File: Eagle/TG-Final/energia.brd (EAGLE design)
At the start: 172.7 x 172.7 mm, 45 parts, among them IC1 7812T, IC2 7805, IC3 AZ1117, IC4 7806T, Q1 TIP2955

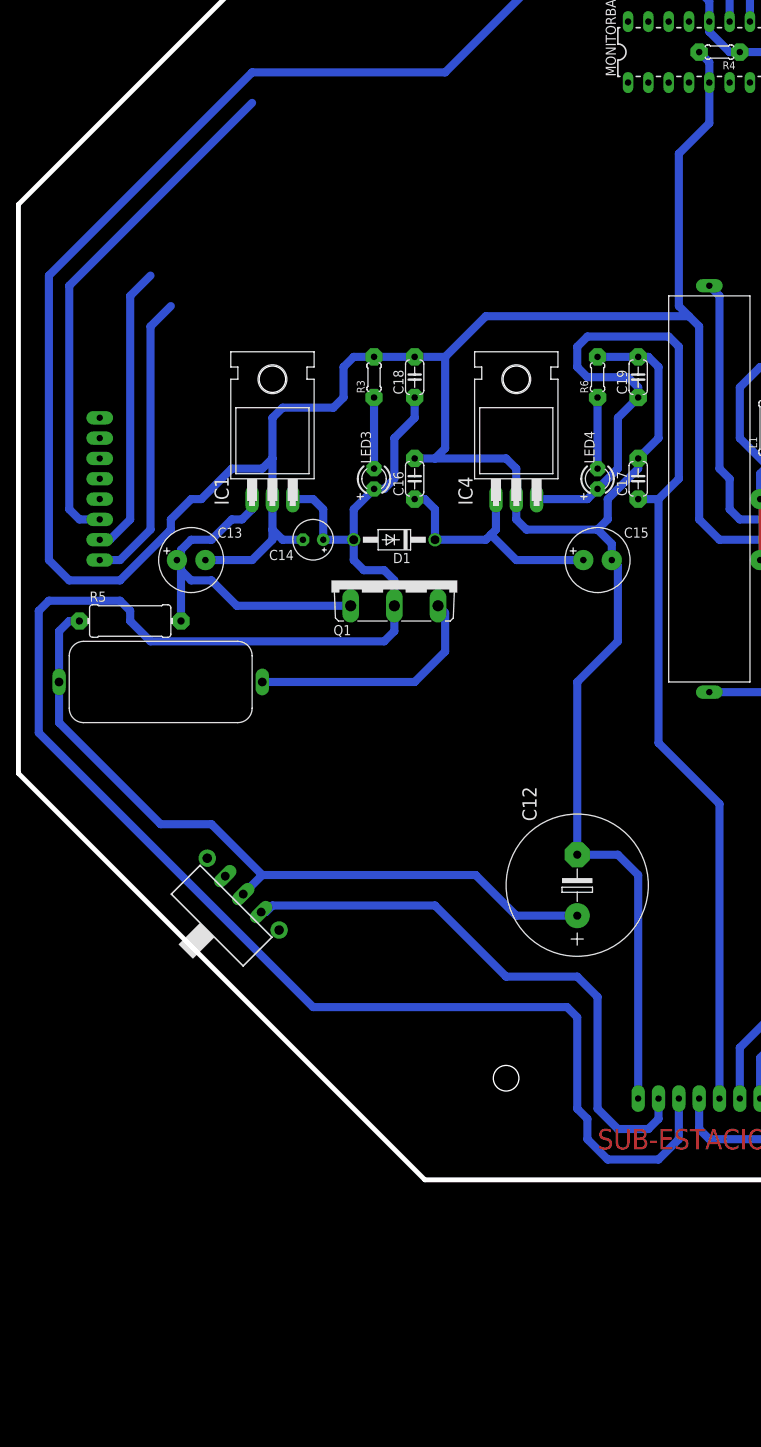
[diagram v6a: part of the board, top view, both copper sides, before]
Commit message: Pruebas del Monitor de Baterias Lipo
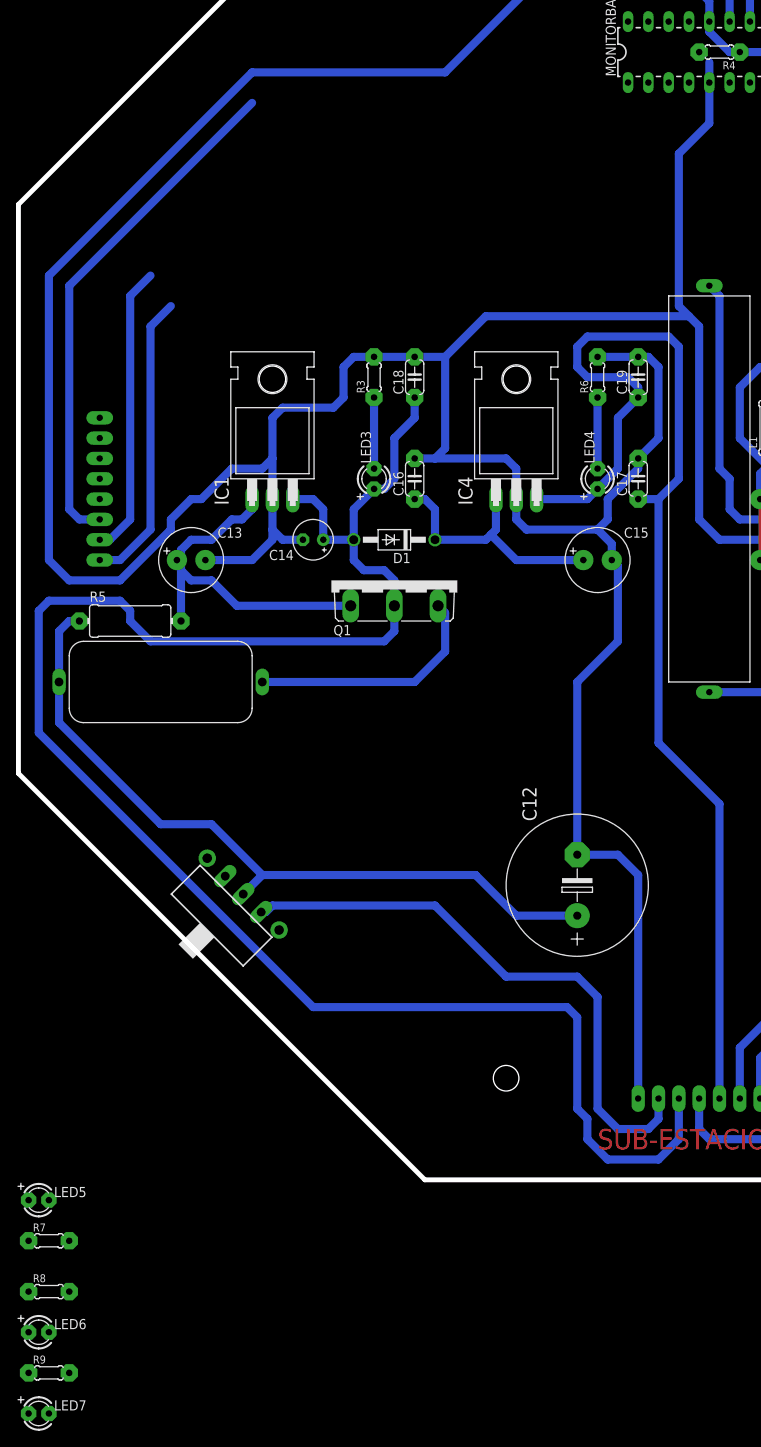
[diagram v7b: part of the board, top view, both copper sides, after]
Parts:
- added LED5, LED6, LED7: (no value), adafruit:LED3MM
- added R7, R8, R9: 470, rcl:0204/5
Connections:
- new net N$15: LED5.K, R7.2
- new net N$16: LED6.K, R8.2
- new net N$19: LED7.K, R9.2
- net N$2: now also R4.2
- net VSS: now also R7.1, R8.1, R9.1; no longer R4.2
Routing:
- net VSS: track 633.6 -> 631.8 mm
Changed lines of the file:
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@@
 <element name="LED4" library="adafruit" package="LED3MM" value="VERDE" x="21.59" y="87.63" rot="R90"/>
 <element name="R6" library="rcl" package="0204/5" value="680" x="21.59" y="100.33" rot="R90"/>
+<element name="LED5" library="adafruit" package="LED3MM" value="" x="-48.26" y="-2.54"/>
+<element name="R7" library="rcl" package="0204/5" value="470" x="-46.99" y="-7.62"/>
+<element name="LED6" library="adafruit" package="LED3MM" value="" x="-48.26" y="-19.05"/>
+<element name="R8" library="rcl" package="0204/5" value="470" x="-46.99" y="-13.97"/>
+<element name="LED7" library="adafruit" package="LED3MM" value="" x="-48.26" y="-29.21"/>
+<element name="R9" library="rcl" package="0204/5" value="470" x="-46.99" y="-24.13"/>
 </elements>
 <signals>
@@
 <contactref element="JP1" pad="4"/>
 <contactref element="MONITORBATERIA" pad="5"/>
-<contactref element="R4" pad="2"/>
 <contactref element="C18" pad="2"/>
 <contactref element="R3" pad="2"/>
@@
 <wire x1="57.15" y1="83.07605" x2="57.15" y2="85.09" width="1.016" layer="16"/>
 <wire x1="35.56" y1="137.16" x2="35.56" y2="139.7" width="1.016" layer="16"/>
-<wire x1="35.56" y1="139.7" x2="34.29" y2="140.97" width="1.016" layer="16"/>
 <wire x1="34.29" y1="152.4" x2="34.29" y2="154.94" width="1.016" layer="16"/>
 <wire x1="34.29" y1="154.94" x2="33.02" y2="156.21" width="1.016" layer="16"/>
@@
 <wire x1="33.02" y1="107.95" x2="31.75" y2="109.22" width="1.016" layer="16"/>
 <wire x1="31.75" y1="109.22" x2="31.75" y2="128.27" width="1.016" layer="16"/>
+<contactref element="R7" pad="1"/>
+<contactref element="R8" pad="1"/>
+<contactref element="R9" pad="1"/>
+<wire x1="-49.53" y1="-13.97" x2="-49.53" y2="-24.13" width="0" layer="19" extent="1-1"/>
+<wire x1="-49.53" y1="-7.62" x2="-49.53" y2="-13.97" width="0" layer="19" extent="1-1"/>
+<wire x1="26.67" y1="10.16" x2="-49.53" y2="-7.62" width="0" layer="19" extent="1-1"/>
 </signal>
 <signal name="+22V">
@@
 <contactref element="JP1" pad="6"/>
 <contactref element="MONITORBATERIA" pad="4"/>
-<wire x1="33.02" y1="137.16" x2="29.21" y2="152.4" width="0" layer="19" extent="1-1"/>
+<contactref element="R4" pad="2"/>
+<wire x1="34.29" y1="140.97" x2="29.21" y2="152.4" width="0" layer="19" extent="1-1"/>
+<wire x1="33.02" y1="137.16" x2="34.29" y2="140.97" width="0" layer="19" extent="1-1"/>
 </signal>
 <signal name="N$5">
@@
 <wire x1="21.59" y1="97.79" x2="21.59" y2="88.9" width="1.016" layer="16"/>
 </signal>
+<signal name="N$15">
+<contactref element="LED5" pad="K"/>
+<contactref element="R7" pad="2"/>
+<wire x1="-46.99" y1="-2.54" x2="-44.45" y2="-7.62" width="0" layer="19" extent="1-1"/>
+</signal>
+<signal name="N$16">
+<contactref element="LED6" pad="K"/>
+<contactref element="R8" pad="2"/>
+<wire x1="-44.45" y1="-13.97" x2="-46.99" y2="-19.05" width="0" layer="19" extent="1-1"/>
+</signal>
+<signal name="N$19">
+<contactref element="LED7" pad="K"/>
+<contactref element="R9" pad="2"/>
+<wire x1="-44.45" y1="-24.13" x2="-46.99" y2="-29.21" width="0" layer="19" extent="1-1"/>
+</signal>
 </signals>

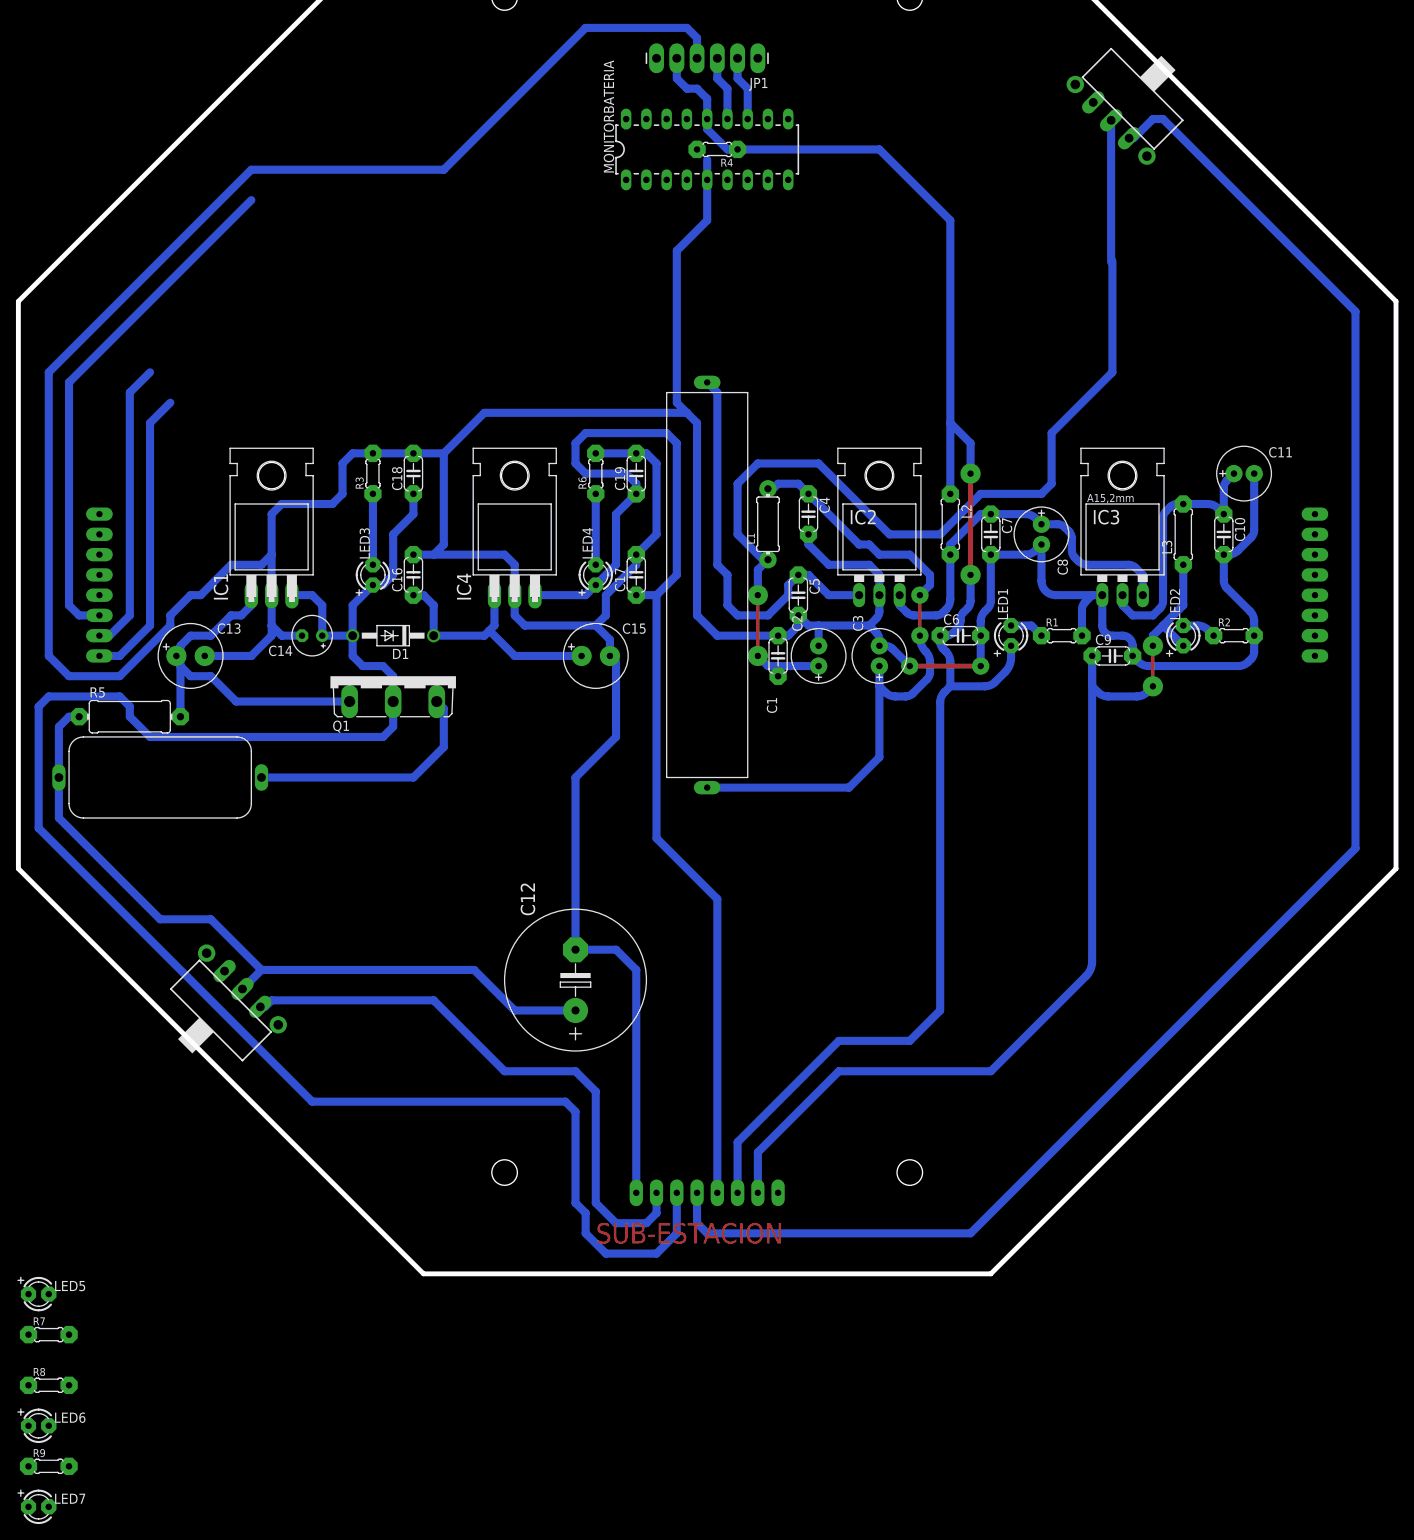
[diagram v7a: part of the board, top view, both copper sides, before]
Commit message: Peliando con un 16f88
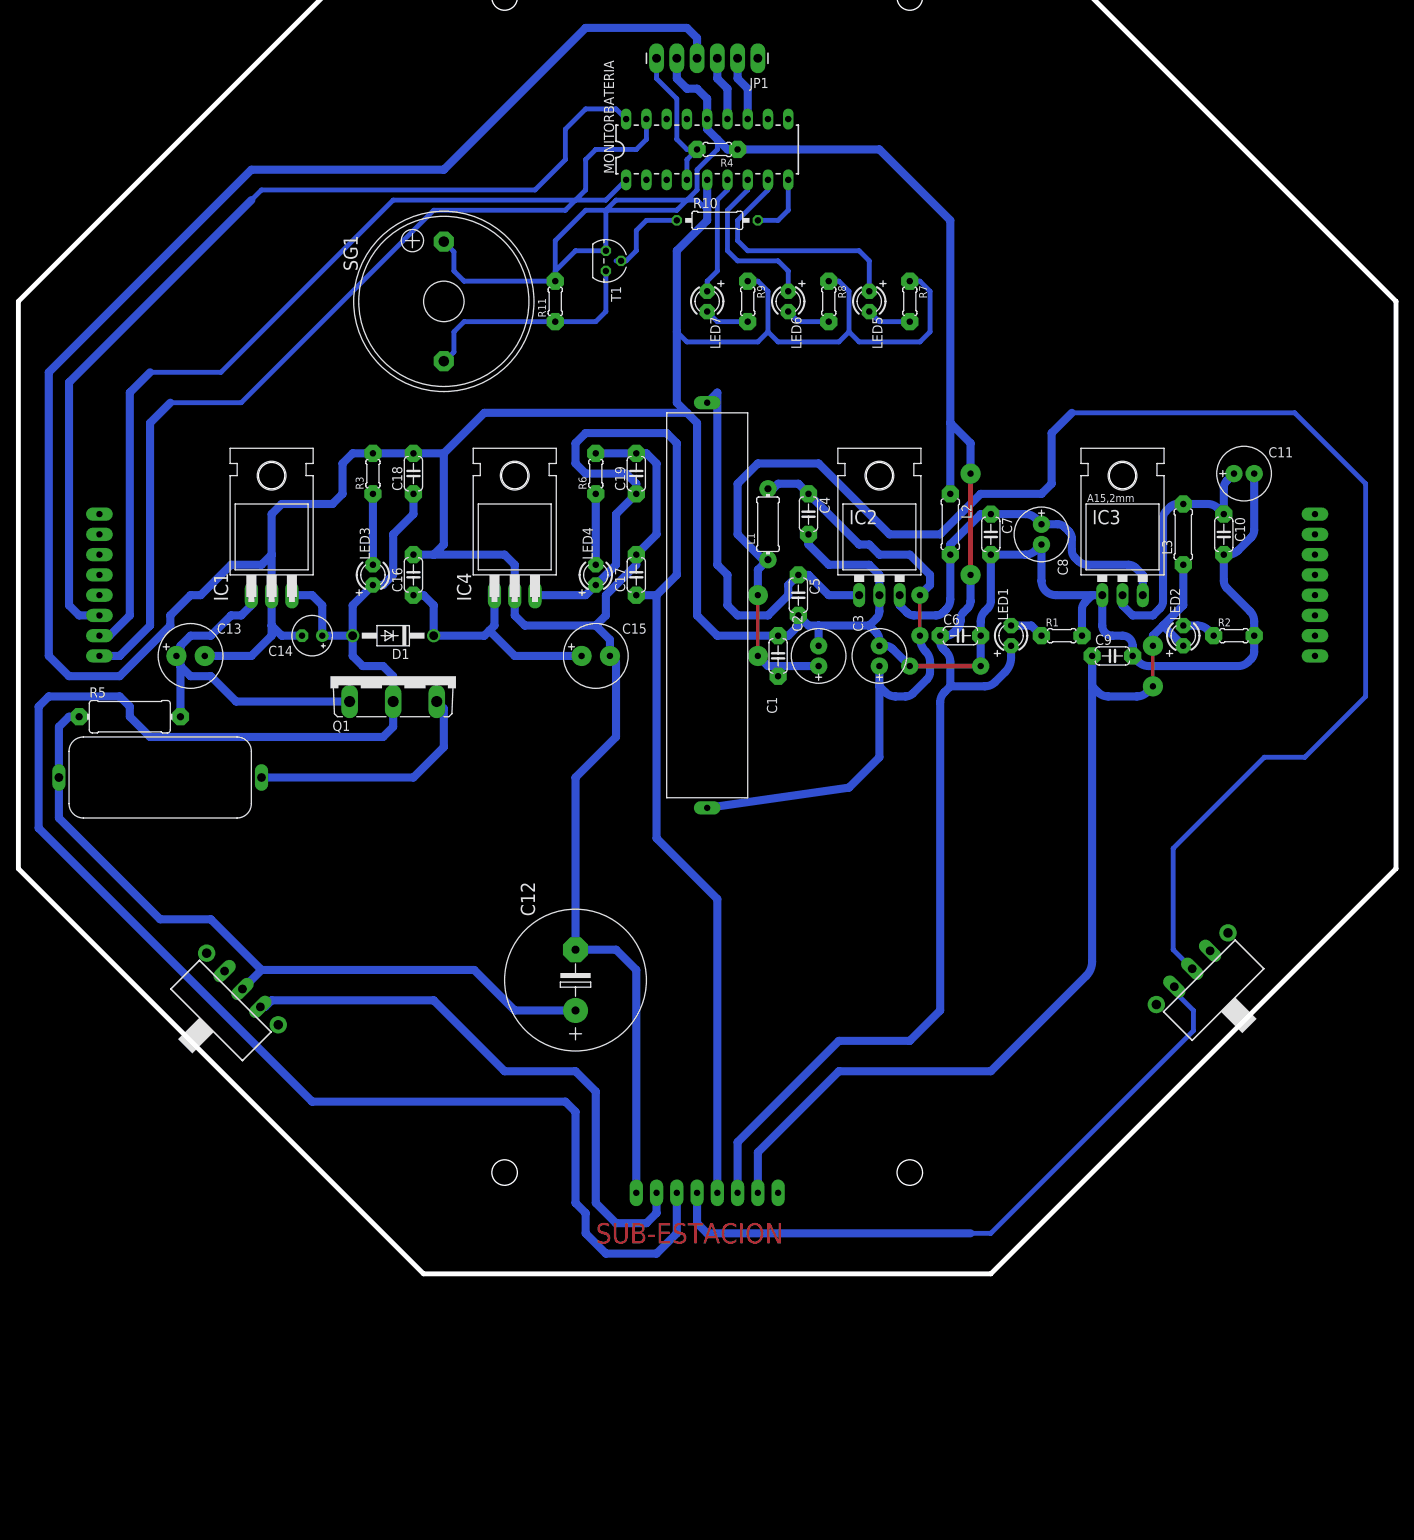
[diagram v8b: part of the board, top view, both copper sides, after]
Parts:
- added R10: 4K7, rcl:0207/10
- added R11: 4K7, rcl:0204/5
- added SG1: EB2209A, buzzer:EB2209A
- added T1: 2N3904, transistor:TO92
- moved LED7 172.8 mm to (35.6, 121.9), turned to 270 degrees
- moved R9 170.3 mm to (40.6, 121.9), turned to 270 degrees
- moved LED6 169.4 mm to (45.7, 121.9), turned to 270 degrees
- moved R7 168.6 mm to (61.0, 121.9), turned to 270 degrees
- moved R8 167.4 mm to (50.8, 121.9), turned to 270 degrees
- moved LED5 162.3 mm to (55.9, 121.9), turned to 270 degrees
- moved S1 112.2 mm to (99.1, 35.6), turned to 225 degrees
- moved U$9 2.54 mm to (35.6, 83.8)
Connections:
- new net N$20: LED7.A, MONITORBATERIA.6
- new net N$21: LED6.A, MONITORBATERIA.7
- new net N$22: LED5.A, MONITORBATERIA.8
- new net N$23: MONITORBATERIA.9, R10.2
- new net N$24: R10.1, T1.2
- new net N$25: R11.1, SG1.-, T1.1
- net VDD: now also R11.2, SG1.+
- net VSS: now also T1.3
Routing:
- net +11V1: track 213.6 -> 83.7 mm
- net SENSE1: track 36.9 -> 115.1 mm
- net N$1: track 129.1 -> 205.4 mm
- net VSS: track 631.8 -> 707.5 mm
- net SENSE3: track 36.4 -> 106.1 mm
- net VDD: track 207.7 -> 266.7 mm
- net SENSE2: track 64.6 -> 119.1 mm
- net N$22: track 0.00 -> 30.6 mm
- net N$25: track 0.00 -> 29.5 mm
- net N$21: track 0.00 -> 21.2 mm
- net N$2: track 0.00 -> 18.6 mm
- net N$20: track 0.00 -> 15.0 mm
- net N$24: track 0.00 -> 11.2 mm
- net N$23: track 0.00 -> 8.15 mm
- net N$19: track 0.00 -> 5.61 mm
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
